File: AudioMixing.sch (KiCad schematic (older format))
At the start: 38 parts

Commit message: - MAX98089 fertig - Footprints von MAX und Oszilator angepasst - Pullups für I2C hinzugefügt - Bus / Signal Namen Fehlzuweisungen ausgebessert
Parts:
- removed C? (x10): 10pF, symbol Device:C
- removed C? (x17): 1uF, symbol Device:C
- removed C?: 10uF, symbol Device:C
- removed C?: 0.1uF, symbol Device:C
- removed C?: 2.2uF, symbol Device:C
- removed C?: 100n, symbol Device:C
- removed R?: 10k, symbol Device:R_US
- added C? (x10): 10p/50V/C0G, Resistor_SMD:R_0603_1608Metric, symbol Device:C
- added C? (x17): 1u/6V3/X5R, Resistor_SMD:R_0603_1608Metric, symbol Device:C
- added C?: 2u2/6V3/X5R, Resistor_SMD:R_0603_1608Metric, symbol Device:C
- added C?: 10u/6V3/X5R, Resistor_SMD:R_0603_1608Metric, symbol Device:C
- added C? (x2): 100n/10V/X7R, Resistor_SMD:R_0603_1608Metric, symbol Device:C
- added R?: 10k/5%, Resistor_SMD:R_0603_1608Metric, symbol Device:R
- R? (x4): value 2.2k -> 2k2/1%; footprint (none) -> Resistor_SMD:R_0603_1608Metric
- U?: footprint 21-0144H_T5677-1_MXM -> TeKaDe:QFN-56_EP_7x7_Pitch0.4mm
- Y?: footprint 830208220101 -> TeKaDe:WE_IQXO-791
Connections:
- net labels removed: I2S2
- wire segments 157 -> 156
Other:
- note added: "Clock Generator MCLK\n12.2880MHz für 48kHz / 11.2896 für 44,1kHz"
- note added: "DVDD / AVDD"
- note added: "DVDDS1"
- note added: "DVDDS2"
- note added: "HPSNS ist GND an Klinkenbuchse, vgl. Fig 40\nJack sensing nicht vorgesehen -> HPSNS direkt an GND\nMic: differential + biasing\n\nÄnderungen:\nI2C Pullups auf RPi Seite machen\nFootprints angepasst\nSPKRVDD auf 3V3, nicht mehr 5V (siehe DS S.126)\nReihen Cs bei Line Out entfernt (siehe Email Maxim 02.07.2021)\nfix: AGND keine Verbindung zu GND\nfix: EPAD auf GND, nicht NC\nfix: bypass C an Oszila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"
- note added: "PVDD"
- note added: "SPKRxVDD"
- note added: "The microphone differential signals (MIC.MAIN.P and MIC.MAIN.N) \nare very low-level and must be balanced and routed \nin parallel, the same distance from start to end, \nthe same impedance for both signals.\n\nFigure 5 and Figure 6 show typical schematics for microphone input. \nThe microphone filtering capacitor must be as close as possible to the mic. \nThe other components must be as close as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"
- note removed: "An SPKRP/N SPKLP/N keine Speaker angeschlossen\n-> Versorgung SPKL/R VDD notwendig?\n=> Ja, laut S.126, aber es reichen auf 3V3"
- note removed: "Line Out?\nHier keine Cs gegen GND wie bei:\n- Line In\n- Headset Out\n-> Orientiert an Referenzdesign, werde ich aber empirisch prüfen"
- note removed: "MCLK ist nicht für I2S!! \n12.2880MHz für 48kHz / 11.2896 für 44,1kHz\nWird diese vom BM83 geliefert? der hat MCLK out???\nHPSNS ist GND an Klinkenbuchse, vgl. Fig 40\nJack sensing nicht vorgesehen -> HPSNS direkt an GND\n\nÄnderungen:\nfix: AGND keine Verbindung zu GND\nfix: EPAD auf GND, nicht NC\nfix: bypass C an Oszilator, wie in Datenblatt gefordert"
- note removed: "Pullups??\n"
- note removed: "So nicht in Appnote fig 40\nDafür in Evkit guide fig 4a"
- note removed: "So nicht in Appnote fig 40\nStattdessen in EvKit guide fig 4a\n-> differential/single ended an EvKit zu prüfen!"
- note removed: "The PreDriv.LEFT and PreDriv.RIGHT signals are the stereo audio output lines. To prevent audio\ndegradation, these signals must be shielded and routed to avoid noise sources, especially those that\ngenerate noise in the audio range.\nTypically, these signals drive external class-D amplifiers, as shown in Figure 8. Resistors Ri and\ncapacitors Ci must be as close as possible to the external class-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"
- note removed: "The microphone differential signals (MIC.MAIN.P and MIC.MAIN.N) are very low-level and must be\nbalanced and routed in parallel, the same distance from start to end, the same impedance for both\nsignals.\nFigure 5 and Figure 6 show typical schematics for microphone input. The microphone filtering capacitor\nmust be as close as possible to the microphone. The other components must be as close as p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"
- moved on the sheet: R?, Y?

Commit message: - BT fertig, warten auf Rueckmeldung von Microchip - CM3 fast fertig - diverse Kleinigkeiten
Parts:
- gave numbers to parts that had none: 38
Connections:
- net Rpi.SCL0 renamed RPi_I2C0_SCL
- net Rpi.SDA0 renamed RPi_I2C0_SDA

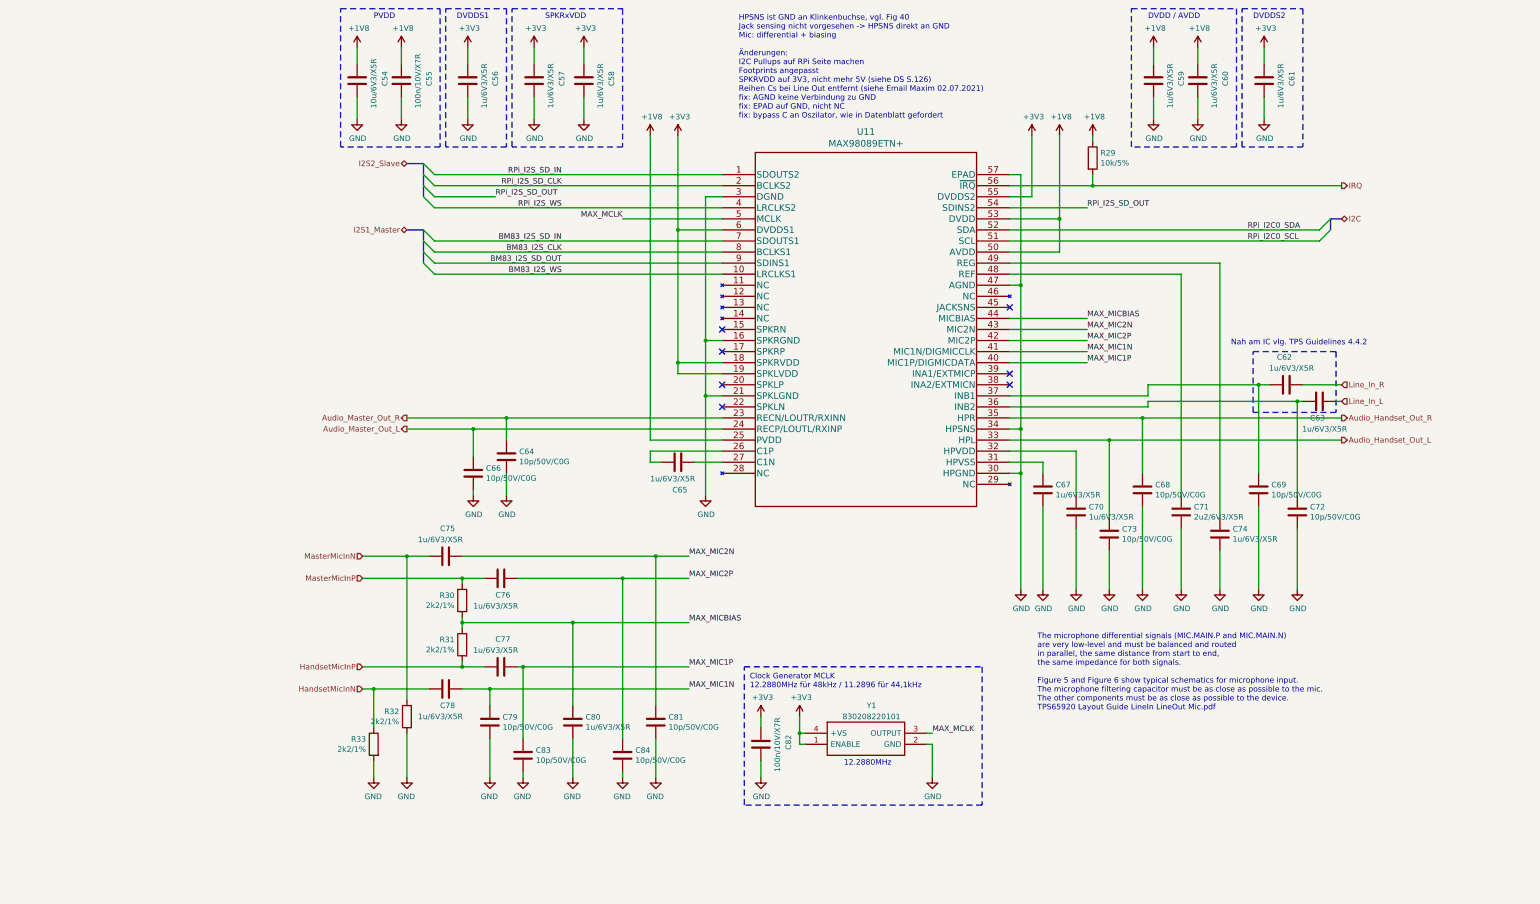
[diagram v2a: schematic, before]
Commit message: - CM3 durch CM4 ersetzt - Spannungsregler für 3,3 und 1,8V entfernt, da nun von CM4 erzeugt - RTC IC getauscht
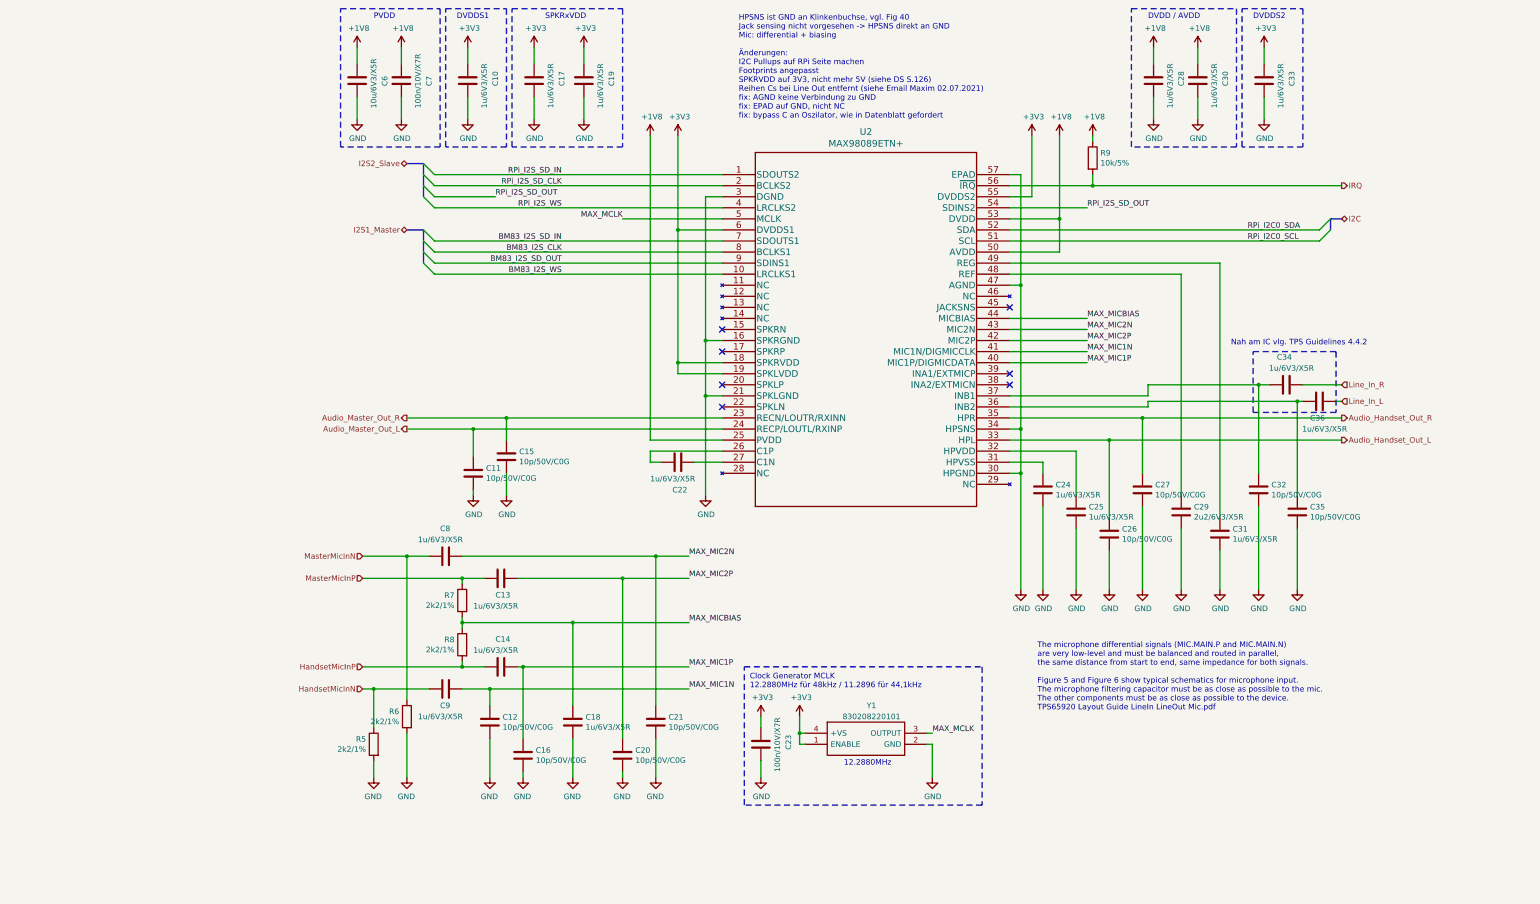
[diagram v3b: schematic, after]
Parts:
- renumbered C56 to C10, C66 to C11, C79 to C12, C76 to C13, C77 to C14, C64 to C15, C83 to C16, C57 to C17, C80 to C18, C58 to C19, C84 to C20, C81 to C21, C65 to C22, C82 to C23, C67 to C24, C70 to C25, C73 to C26, C68 to C27, C59 to C28, C71 to C29, C60 to C30, C74 to C31, C69 to C32, C61 to C33, C62 to C34, C72 to C35, C63 to C36, C54 to C6, C55 to C7, C75 to C8, C78 to C9, R33 to R5, R32 to R6, R30 to R7, R31 to R8, R29 to R9, U11 to U2
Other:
- note added: "The microphone differential signals (MIC.MAIN.P and MIC.MAIN.N) \nare very low-level and must be balanced and routed in parallel,\nthe same distance from start to end, same impedance for both signals.\n\nFigure 5 and Figure 6 show typical schematics for microphone input. \nThe microphone filtering capacitor must be as close as possible to the mic. \nThe other components must be as close as possib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"
- note removed: "The microphone differential signals (MIC.MAIN.P and MIC.MAIN.N) \nare very low-level and must be balanced and routed \nin parallel, the same distance from start to end, \nthe same impedance for both signals.\n\nFigure 5 and Figure 6 show typical schematics for microphone input. \nThe microphone filtering capacitor must be as close as possible to the mic. \nThe other components must be as close as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"

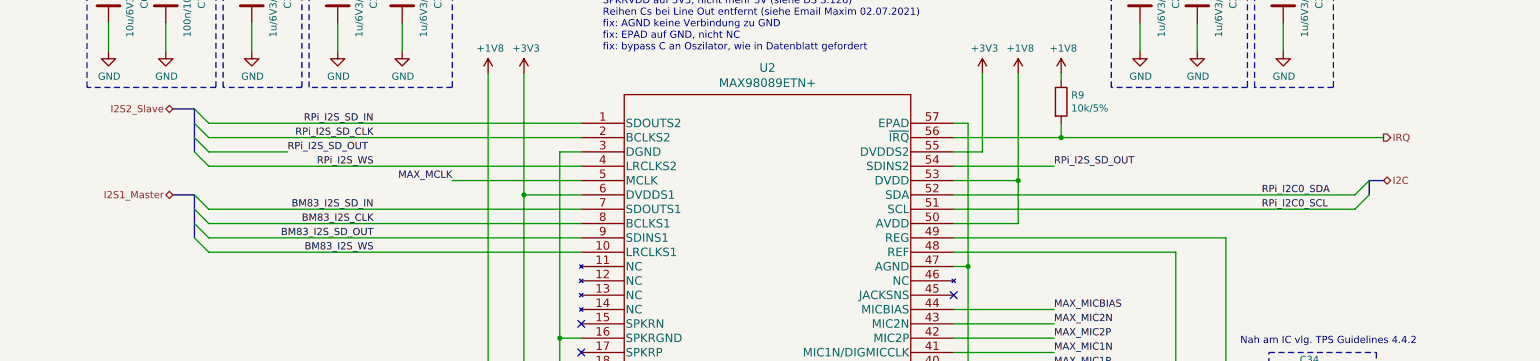
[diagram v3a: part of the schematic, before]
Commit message: - Bus Topologie entfernt - Levelshifter auf eigenes Blatt, abgeschlossen
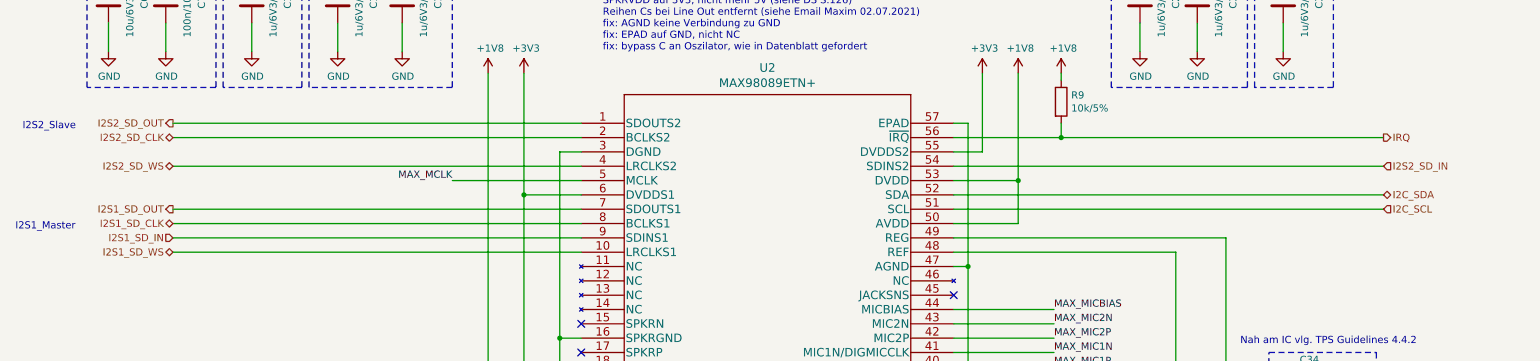
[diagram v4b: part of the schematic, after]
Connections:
- net BM83_I2S_CLK renamed I2S1_SD_CLK
- net BM83_I2S_SD_IN renamed I2S1_SD_OUT
- net BM83_I2S_SD_OUT renamed I2S1_SD_IN
- net BM83_I2S_WS renamed I2S1_SD_WS
- net RPi_I2C0_SCL renamed I2C_SCL
- net RPi_I2C0_SDA renamed I2C_SDA
- net RPi_I2S_SD_CLK renamed I2S2_SD_CLK
- net RPi_I2S_SD_IN renamed I2S2_SD_OUT
- net RPi_I2S_SD_OUT renamed I2S2_SD_IN
- net RPi_I2S_WS renamed I2S2_SD_WS
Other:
- note added: "I2S1_Master"
- note added: "I2S2_Slave"
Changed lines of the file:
@@
 $Descr A4 11693 8268
 encoding utf-8
-Sheet 3 8
+Sheet 9 9
 Title ""
 Date ""
@@
 	7900 2050 7900 2150
 Connection ~ 7900 2150
-Text Label 9300 2550 0    50   ~ 0
-RPi_I2C0_SDA
-Text Label 9300 2650 0    50   ~ 0
-RPi_I2C0_SCL
 NoConn ~ 7150 3850
 NoConn ~ 7150 3950
@@
 Text HLabel 10150 2150 2    50   Output ~ 0
 IRQ
-Text Label 7850 2350 0    50   ~ 0
-RPi_I2S_SD_OUT
-Text Label 3100 2050 2    50   ~ 0
-RPi_I2S_SD_IN
-Text Label 3100 2350 2    50   ~ 0
-RPi_I2S_WS
-Text Label 3100 2150 2    50   ~ 0
-RPi_I2S_SD_CLK
-Text HLabel 1700 1950 0    50   BiDi ~ 0
-I2S2_Slave
-Entry Wire Line
-	1850 1950 1950 2050
-Wire Wire Line
-	1950 2050 4550 2050
-Entry Wire Line
-	1850 2050 1950 2150
-Wire Wire Line
-	1950 2150 4550 2150
-Entry Wire Line
-	1850 2250 1950 2350
-Wire Wire Line
-	1950 2350 4550 2350
-Wire Bus Line
-	1850 1950 1700 1950
-Wire Wire Line
-	7850 2350 7150 2350
-Text HLabel 1700 2550 0    50   BiDi ~ 0
-I2S1_Master
-Entry Wire Line
-	1850 2550 1950 2650
-Entry Wire Line
-	1850 2650 1950 2750
-Wire Bus Line
-	1850 2550 1700 2550
-Wire Wire Line
-	1950 2650 4550 2650
-Wire Wire Line
-	1950 2750 4550 2750
-Text Label 3100 2650 2    50   ~ 0
-BM83_I2S_SD_IN
-Text Label 3100 2750 2    50   ~ 0
-BM83_I2S_CLK
-Text Label 3100 2850 2    50   ~ 0
-BM83_I2S_SD_OUT
-Text Label 3100 2950 2    50   ~ 0
-BM83_I2S_WS
-Entry Wire Line
-	1850 2750 1950 2850
-Entry Wire Line
-	1850 2850 1950 2950
-Wire Wire Line
-	1950 2950 4550 2950
-Wire Wire Line
-	1950 2850 4550 2850
+Wire Wire Line
+	1700 2050 4550 2050
+Wire Wire Line
+	1700 2150 4550 2150
+Wire Wire Line
+	1700 2350 4550 2350
+Wire Wire Line
+	10150 2350 7150 2350
+Wire Wire Line
+	1700 2650 4550 2650
+Wire Wire Line
+	1700 2750 4550 2750
+Wire Wire Line
+	1700 2850 4550 2850
 $Comp
 L power:GND #PWR030
@@
 Wire Wire Line
 	2600 4750 2600 4950
-Entry Wire Line
-	10050 2550 9950 2650
-Entry Wire Line
-	10050 2450 9950 2550
-Text HLabel 10150 2450 2    50   BiDi ~ 0
-I2C
-Wire Bus Line
-	10050 2550 10050 2450
-Wire Bus Line
-	10050 2450 10150 2450
 Wire Notes Line
 	9350 3650 10100 3650
@@
 $EndComp
 Wire Wire Line
-	7150 2550 9950 2550
-Wire Wire Line
-	7150 2650 9950 2650
+	7150 2550 10150 2550
+Wire Wire Line
+	7150 2650 10150 2650
 Wire Wire Line
 	7900 2150 10150 2150
@@
 	1    0    0    -1
 $EndComp
-Entry Wire Line
-	1950 2250 1850 2150
-Text Label 2500 2250 0    50   ~ 0
-RPi_I2S_SD_OUT
-Wire Wire Line
-	2500 2250 1950 2250
-Wire Bus Line
-	1850 2550 1850 2850
-Wire Bus Line
-	1850 1950 1850 2250
+Text HLabel 10150 2550 2    50   BiDi ~ 0
+I2C_SDA
+Text HLabel 10150 2650 2    50   Input ~ 0
+I2C_SCL
+Text HLabel 1700 2850 0    50   Input ~ 0
+I2S1_SD_IN
+Text HLabel 1700 2650 0    50   Output ~ 0
+I2S1_SD_OUT
+Text HLabel 1700 2750 0    50   BiDi ~ 0
+I2S1_SD_CLK
+Wire Wire Line
+	1700 2950 4550 2950
+Text HLabel 1700 2950 0    50   BiDi ~ 0
+I2S1_SD_WS
+Text Notes 650  2100 0    50   ~ 0
+I2S2_Slave
+Text Notes 600  2800 0    50   ~ 0
+I2S1_Master
+Text HLabel 10150 2350 2    50   Input ~ 0
+I2S2_SD_IN
+Text HLabel 1700 2050 0    50   Output ~ 0
+I2S2_SD_OUT
+Text HLabel 1700 2150 0    50   BiDi ~ 0
+I2S2_SD_CLK
+Text HLabel 1700 2350 0    50   BiDi ~ 0
+I2S2_SD_WS
 $EndSCHEMATC

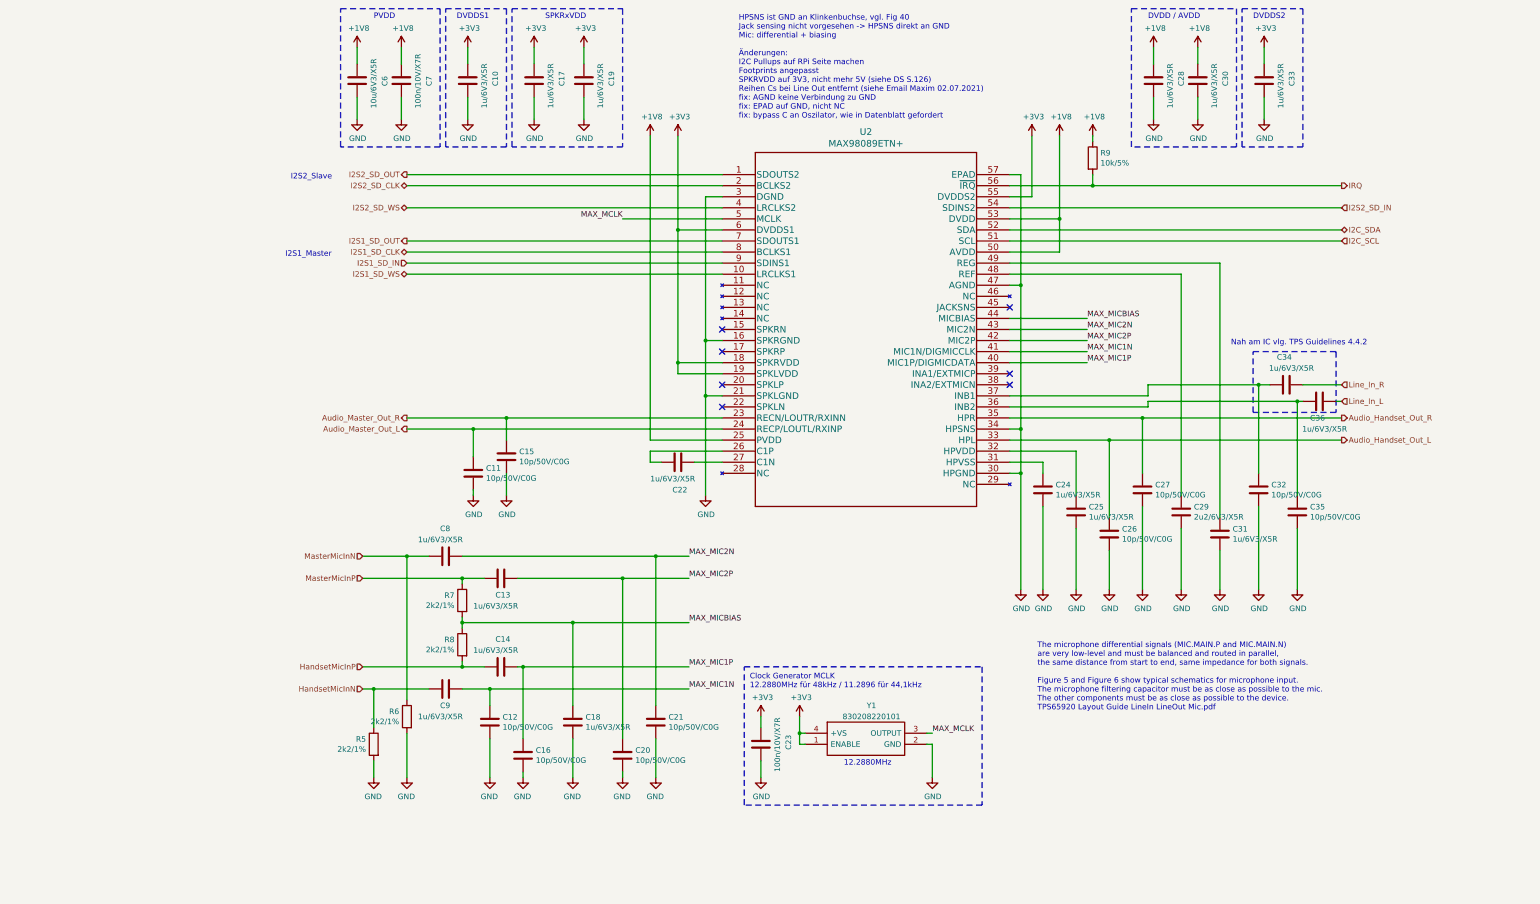
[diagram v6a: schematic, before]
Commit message: - ATmega überarbeitet - Alle offenen Punkte zusammengefasst
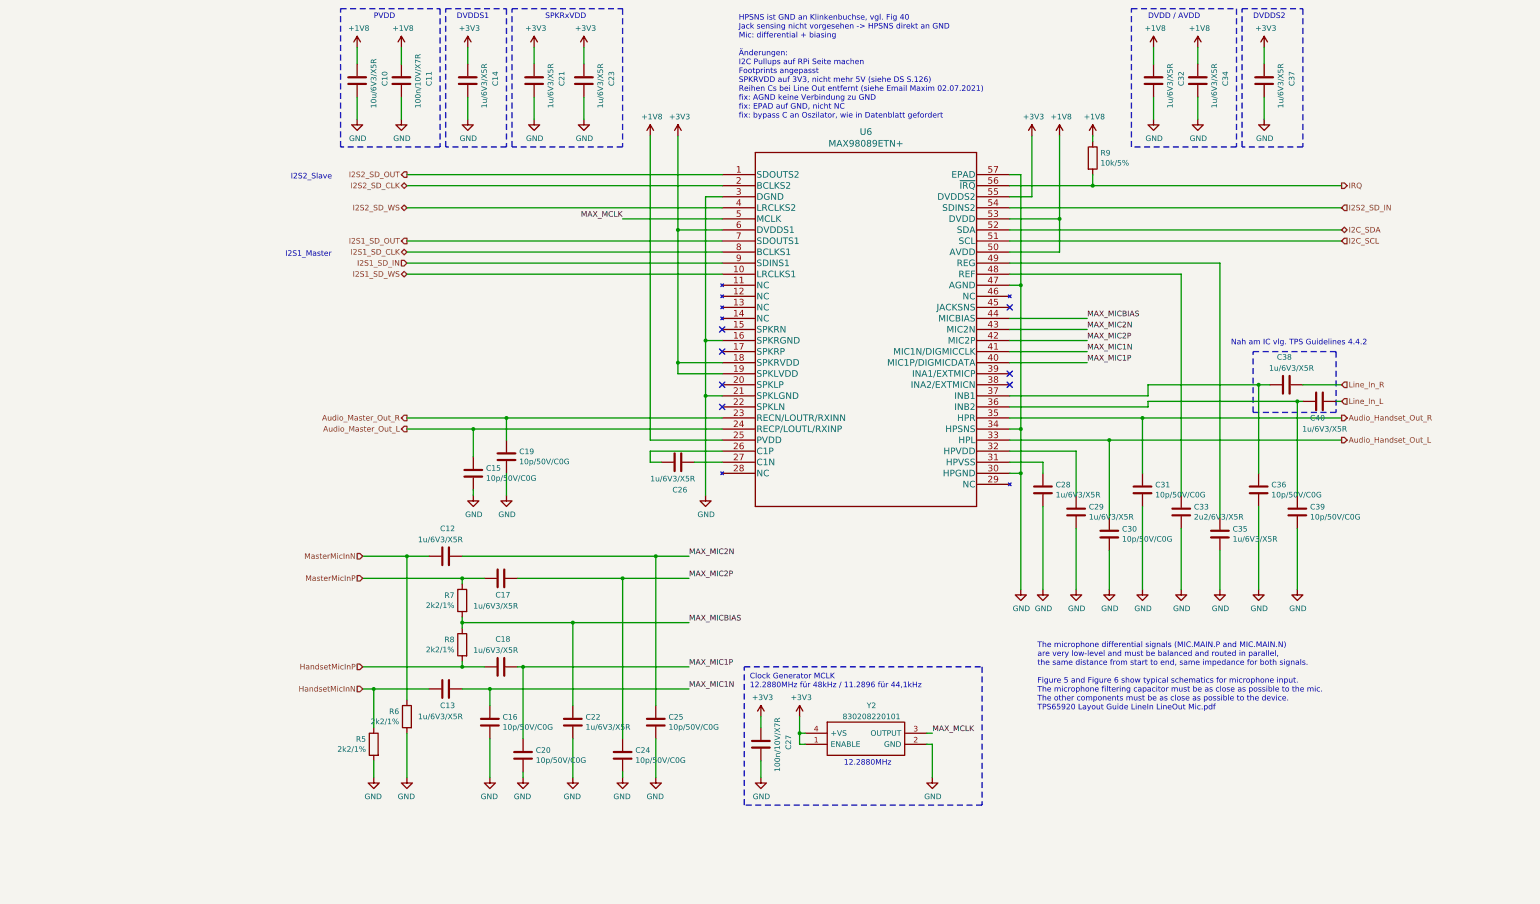
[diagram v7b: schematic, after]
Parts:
- renumbered C6 to C10, C7 to C11, C8 to C12, C9 to C13, C10 to C14, C11 to C15, C12 to C16, C13 to C17, C14 to C18, C15 to C19, C16 to C20, C17 to C21, C18 to C22, C19 to C23, C20 to C24, C21 to C25, C22 to C26, C23 to C27, C24 to C28, C25 to C29, C26 to C30, C27 to C31, C28 to C32, C29 to C33, C30 to C34, C31 to C35, C32 to C36, C33 to C37, C34 to C38, C35 to C39, C36 to C40, U2 to U6, Y1 to Y2
